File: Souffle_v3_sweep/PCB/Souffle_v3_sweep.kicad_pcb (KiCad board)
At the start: 2 copper layers, 137.2 x 114.5 mm, 84 parts, among them J1 LED, J2 4PIN, J3 OLED, J4 Conn_01x01_Female, J5 Conn_01x01_Female, SW1 SW_PUSH, SW10 SW_PUSH, SW11 SW_PUSH, SW12 SW_PUSH, SW13 SW_PUSH, SW14 SW_PUSH, SW15 SW_PUSH, SW16 SW_PUSH, SW17 SW_PUSH, SW18 SW_PUSH, SW19 SW_PUSH, SW2 SW_PUSH, SW20 SW_PUSH, SW21 SW_PUSH, SW22 SW_PUSH, SW23 SW_PUSH, SW24 SW_PUSH, SW25 SW_PUSH, SW25b1 RotaryEncoder_Switch, SW26 SW_PUSH, SW27 SW_PUSH, SW28 SW_PUSH, SW29 SW_PUSH, SW3 SW_PUSH, SW30 SW_PUSH, SW31 SW_SPDT, SW4 SW_PUSH, SW5 SW_PUSH, SW6 SW_PUSH, SW7 SW_PUSH, SW8 SW_PUSH, SW9 SW_PUSH, U1 ProMicro

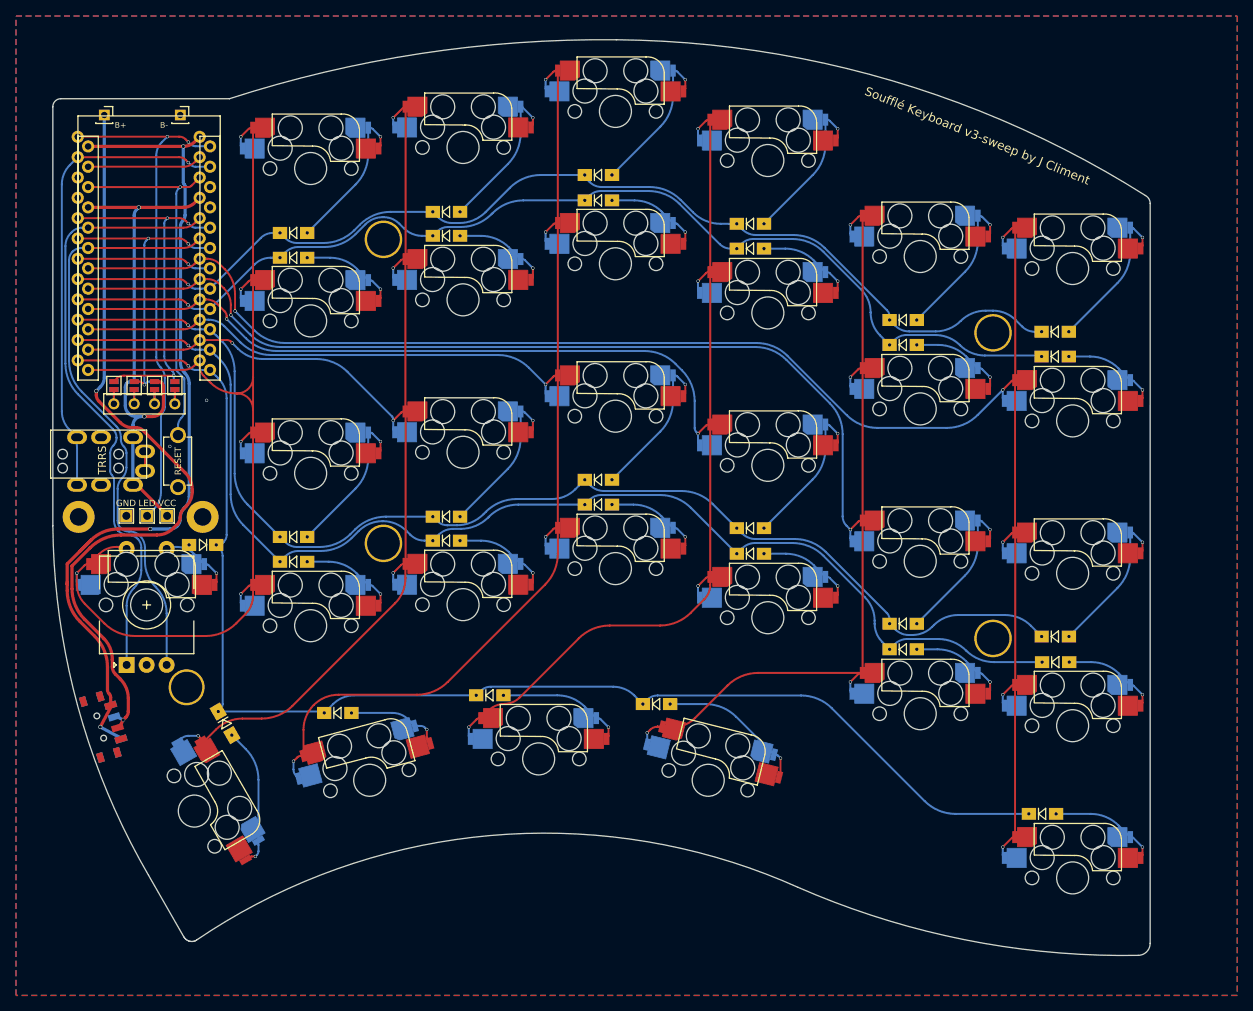
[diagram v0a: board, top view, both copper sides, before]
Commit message: Update tracks and moved boards to KiCad 7.x
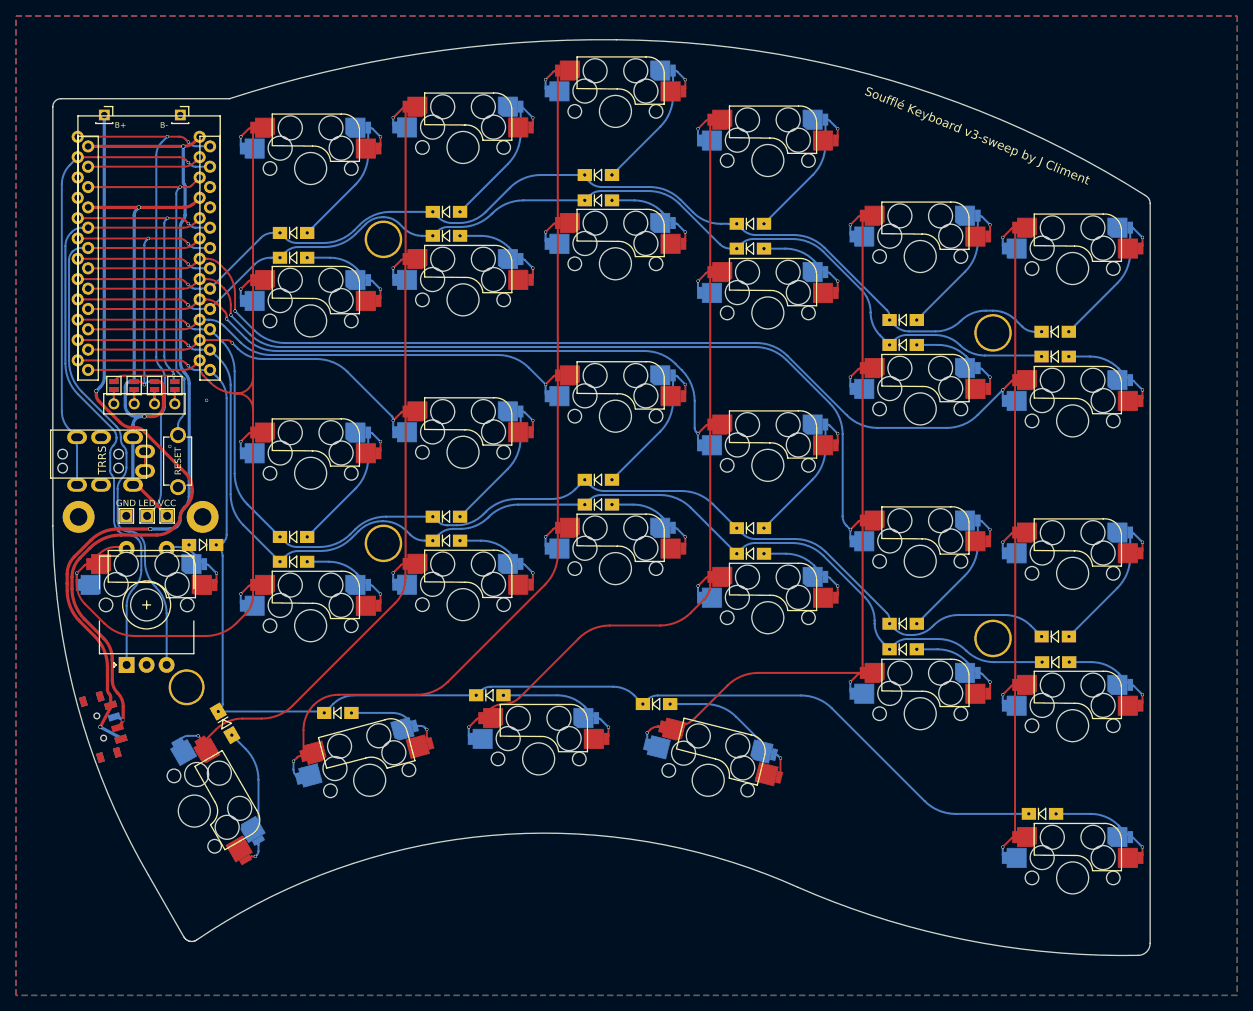
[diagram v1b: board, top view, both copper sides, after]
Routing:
- net col2: track 198.5 -> 192.8 mm
- net row2: track 153.2 -> 147.9 mm
- net col1: track 219.5 -> 214.5 mm
- net SW25A: track 138.2 -> 133.7 mm
- net row4: track 169.4 -> 164.9 mm
- net col3: track 185.3 -> 181.3 mm
- net col4: track 153.2 -> 150.5 mm
- net RAW: track 105.7 -> 103.0 mm
- net Net-(D26-Pad2): track 17.8 -> 15.2 mm
- net col0: track 219.9 -> 217.9 mm
- net row1: track 137.3 -> 135.6 mm
- net VCC: track 65.5 -> 64.0 mm
- net BAT: track 96.8 -> 95.5 mm
- net row0: track 136.1 -> 134.8 mm
- net SW25B: track 12.3 -> 11.1 mm
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
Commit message: Updated OLED connection to accomodate for NiceView option.
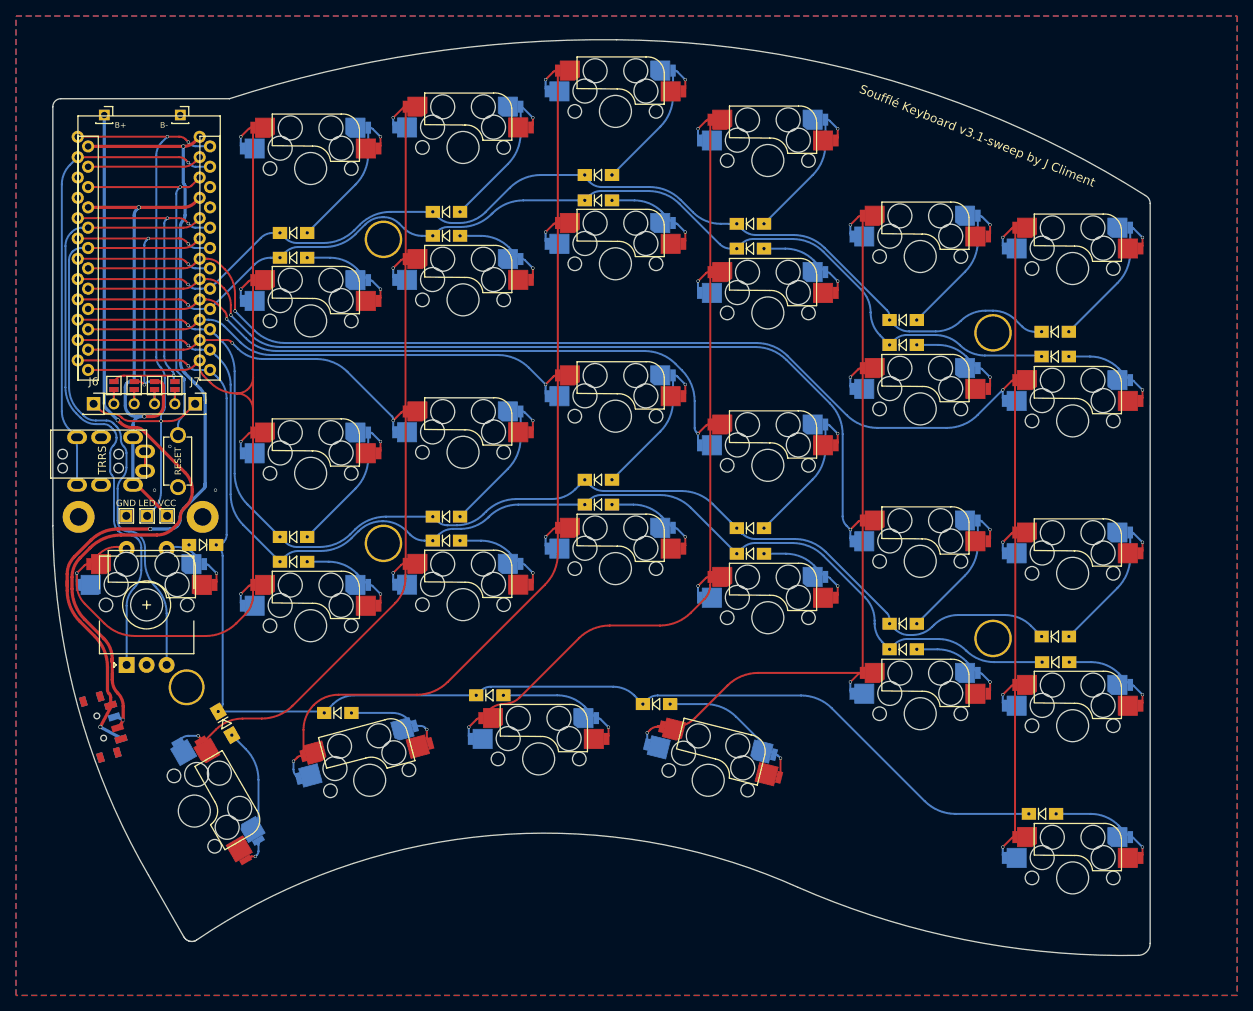
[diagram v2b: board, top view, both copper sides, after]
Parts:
- added J6: Conn_01x01, Connector_PinSocket_2.54mm:PinSocket_1x01_P2.54mm_Vertical, F.Cu at (79.0, 74.8)
- added J7: Conn_01x01, Connector_PinSocket_2.54mm:PinSocket_1x01_P2.54mm_Vertical, F.Cu at (91.7, 74.8)
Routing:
- net LED: track 65.8 -> 79.0 mm, vias 2 -> 3
- net SW25B: track 11.1 -> 8.37 mm
- net RAW: track 103.0 -> 104.7 mm
- net ENCB: track 73.3 -> 74.8 mm
- net ENCA: track 75.6 -> 77.0 mm
- net BAT: track 95.5 -> 94.7 mm
- net GND: vias 2 -> 3
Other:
- board text added: "Soufflé Keyboard v3.1-sweep by J Climent"
- board text removed: "Soufflé Keyboard v3-sweep by J Climent"

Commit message: V3.2 of the Soufflé keyboard, with reworked NiceView pins
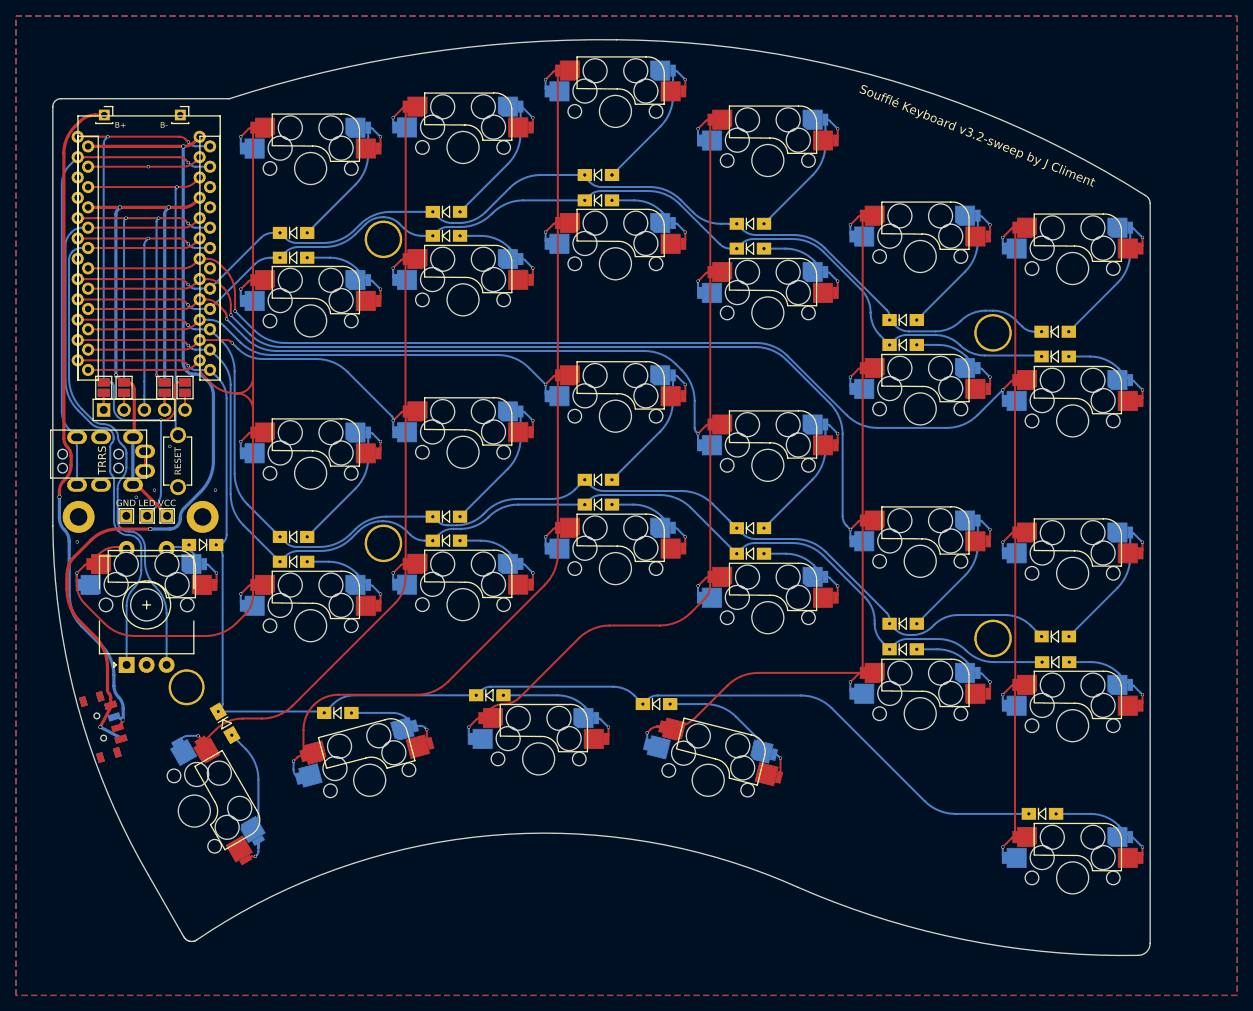
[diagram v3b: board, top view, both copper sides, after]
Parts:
- removed J3: OLED, SofleKeyboard-footprint:OLED_4Pin
- removed J6, J7: Conn_01x01, Connector_PinSocket_2.54mm:PinSocket_1x01_P2.54mm_Vertical
- removed JP1, JP2, JP3, JP4, JP5, JP6, JP7, JP8: SolderJumper_2_Open, SofleKeyboard-footprint:Jumper
- added J9: Conn_01x05_MountingPin, Connector_PinHeader_2.54mm:PinHeader_1x05_P2.54mm_Vertical, F.Cu at (80.3, 75.6)
- added JP10: SolderJumper_2_Open, Jumper:SolderJumper-2_P1.3mm_Open_Pad1.0x1.5mm, B.Cu at (87.9, 72.8)
- added JP12: SolderJumper_2_Open, Jumper:SolderJumper-2_P1.3mm_Open_Pad1.0x1.5mm, B.Cu at (82.8, 72.8)
- added JP13: SolderJumper_2_Open, Jumper:SolderJumper-2_P1.3mm_Open_Pad1.0x1.5mm, B.Cu at (80.3, 72.8)
- added JP14: SolderJumper_2_Open, Jumper:SolderJumper-2_P1.3mm_Open_Pad1.0x1.5mm, F.Cu at (90.4, 72.8)
- added JP15: SolderJumper_2_Open, Jumper:SolderJumper-2_P1.3mm_Open_Pad1.0x1.5mm, F.Cu at (87.9, 72.8)
- added JP17: SolderJumper_2_Open, Jumper:SolderJumper-2_P1.3mm_Open_Pad1.0x1.5mm, F.Cu at (82.8, 72.8)
- added JP18: SolderJumper_2_Open, Jumper:SolderJumper-2_P1.3mm_Open_Pad1.0x1.5mm, F.Cu at (80.3, 72.8)
- added JP9: SolderJumper_2_Open, Jumper:SolderJumper-2_P1.3mm_Open_Pad1.0x1.5mm, B.Cu at (90.4, 72.8)
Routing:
- net unconnected-(U1-D4(PD4)-Pad7)_0: track 16.9 -> 0.00 mm, vias 1 -> 0
- net VCC: track 64.0 -> 77.3 mm, vias 2 -> 3
- net SDA: track 45.5 -> 58.5 mm, vias 3 -> 4
- net BAT: track 94.7 -> 83.4 mm
- net Net-(J9-Pin_5): track 0.00 -> 4.29 mm
- net Net-(J9-Pin_4): track 0.00 -> 4.29 mm
- net Net-(J9-Pin_2): track 0.00 -> 4.29 mm
- net Net-(J9-Pin_1): track 0.00 -> 4.29 mm
- net Net-(J3-P4): track 3.57 -> 0.00 mm
- net Net-(J3-P3): track 3.57 -> 0.00 mm
- net Net-(J3-P2): track 3.57 -> 0.00 mm
- net Net-(J3-P1): track 3.57 -> 0.00 mm
- net RESET: track 46.1 -> 45.1 mm
- net RAW: track 104.7 -> 105.7 mm
- net ENCA: track 77.0 -> 76.2 mm
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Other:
- board text added: "Soufflé Keyboard v3.2-sweep by J Climent"
- board text removed: "Soufflé Keyboard v3.1-sweep by J Climent"

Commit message: Updated and fixed v3.2 as the order of the pads was incorrect. Release v3.2.1 with the fix.
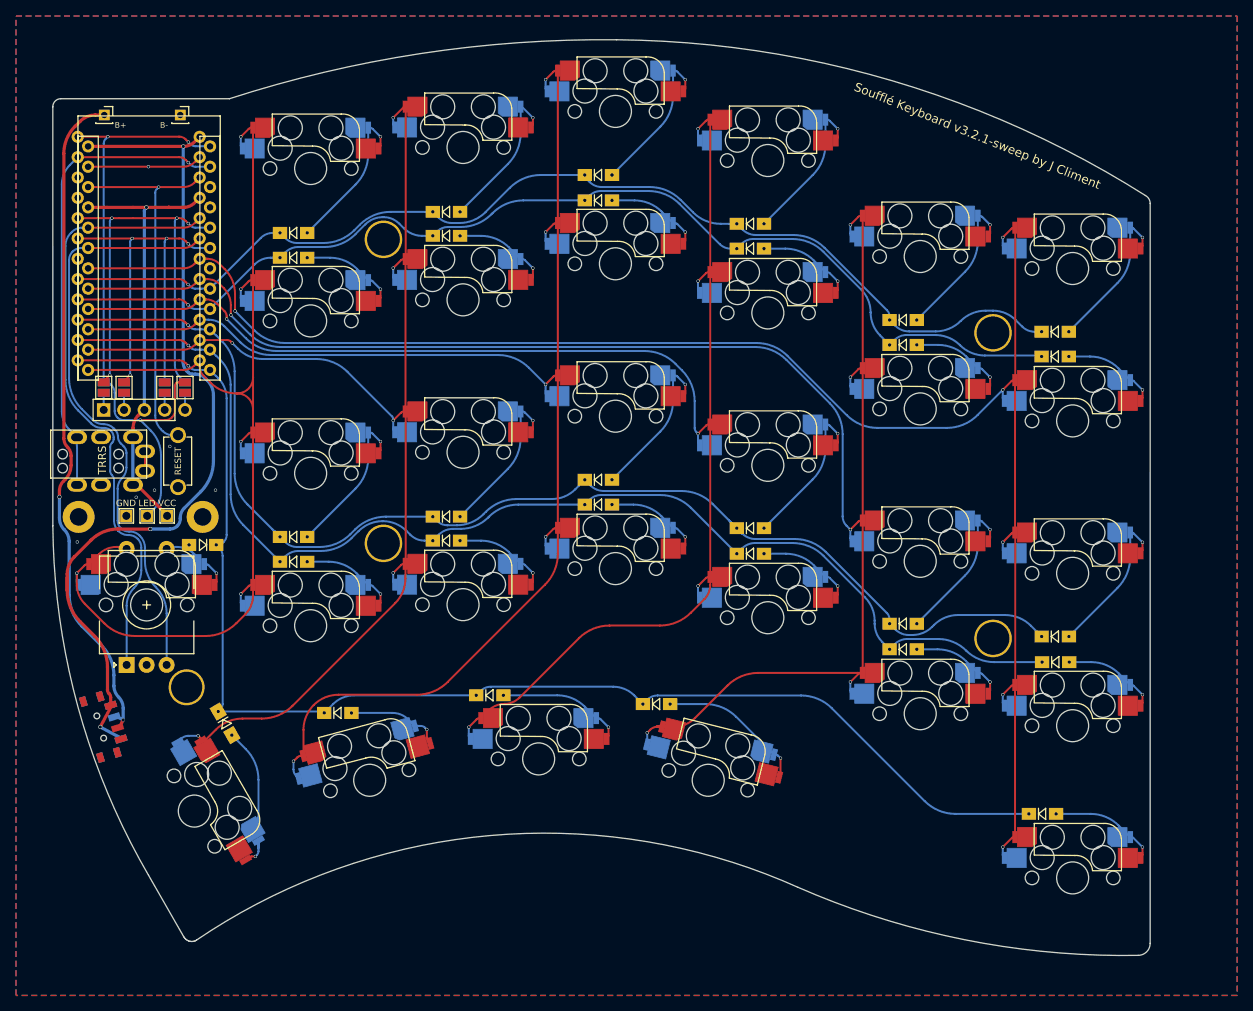
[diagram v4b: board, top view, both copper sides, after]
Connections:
- J9 pad 3: SCL -> VCC
- JP10 pad 2: VCC -> SCL
- JP12 pad 2: SDA -> GND
- JP15 pad 2: SDA -> GND
- JP17 pad 2: VCC -> SCL
- JP18 pad 2: GND -> SDA
- JP9 pad 2: GND -> SDA
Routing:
- net VCC: track 77.3 -> 54.6 mm, vias 3 -> 1
- net SCL: track 38.5 -> 53.4 mm, vias 2 -> 4
- net RESET: track 45.1 -> 47.3 mm
- net Net-(J9-Pin_5): track 4.29 -> 2.14 mm
- net Net-(J9-Pin_4): track 4.29 -> 2.14 mm
- net Net-(J9-Pin_2): track 4.29 -> 2.14 mm
- net Net-(J9-Pin_1): track 4.29 -> 2.14 mm
- net LED: track 78.3 -> 78.9 mm
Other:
- board text added: "Soufflé Keyboard v3.2.1-sweep by J Climent"
- board text removed: "Soufflé Keyboard v3.2-sweep by J Climent"
